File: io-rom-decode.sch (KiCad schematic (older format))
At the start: 9 parts, among them IC25 74LS02, IC26 74LS138, IC27 74LS21, IC27 74LS27, IC28 74LS20, IC29 74LS27, IC82 74LS138, IC83 74LS32

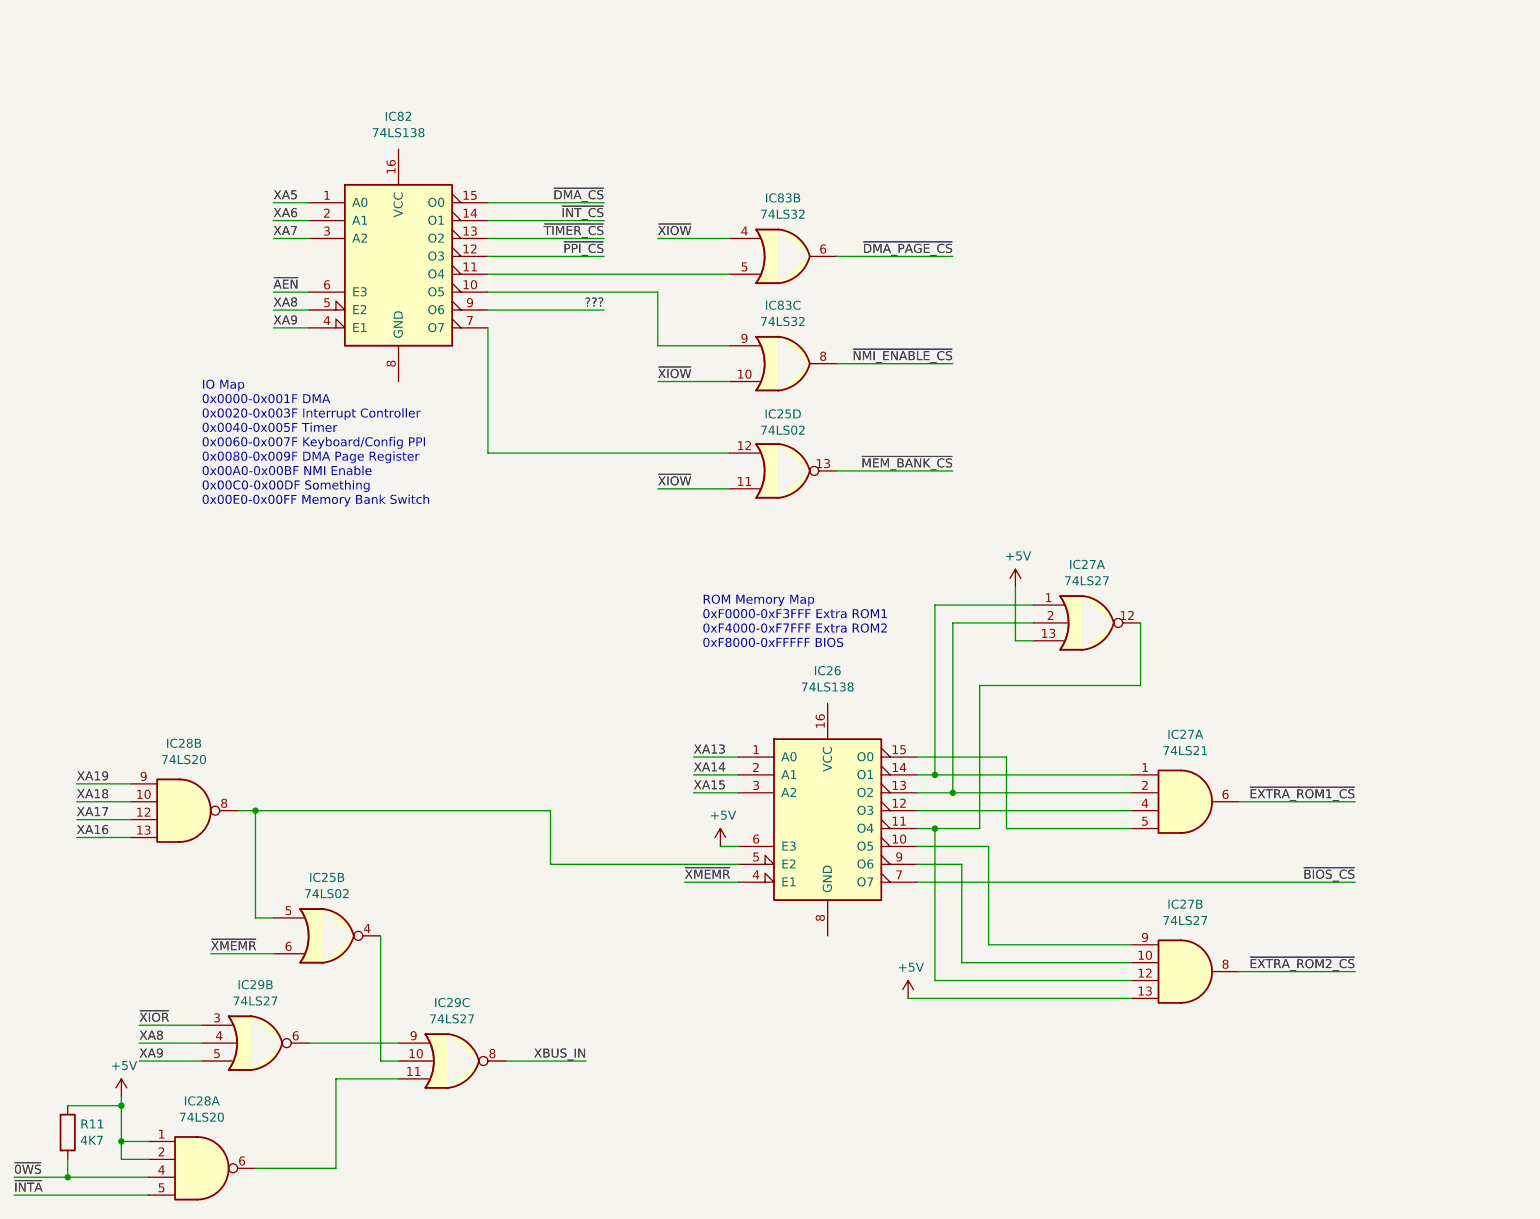
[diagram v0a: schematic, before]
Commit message: Tidy up and map all signals
This fixes up the schematic to:
 - Look presentable
 - Fix all labels connecting sheets
 - Tidy up all loose ends by either inspecting the PCB under
    magnification, measuring with an oscillosope or buzzing
    out with a meter
 - Pass ERC (with 1 exception due to incorrect circuitry around
    pin 33 on the FPU (~RQ~/~GT1~)
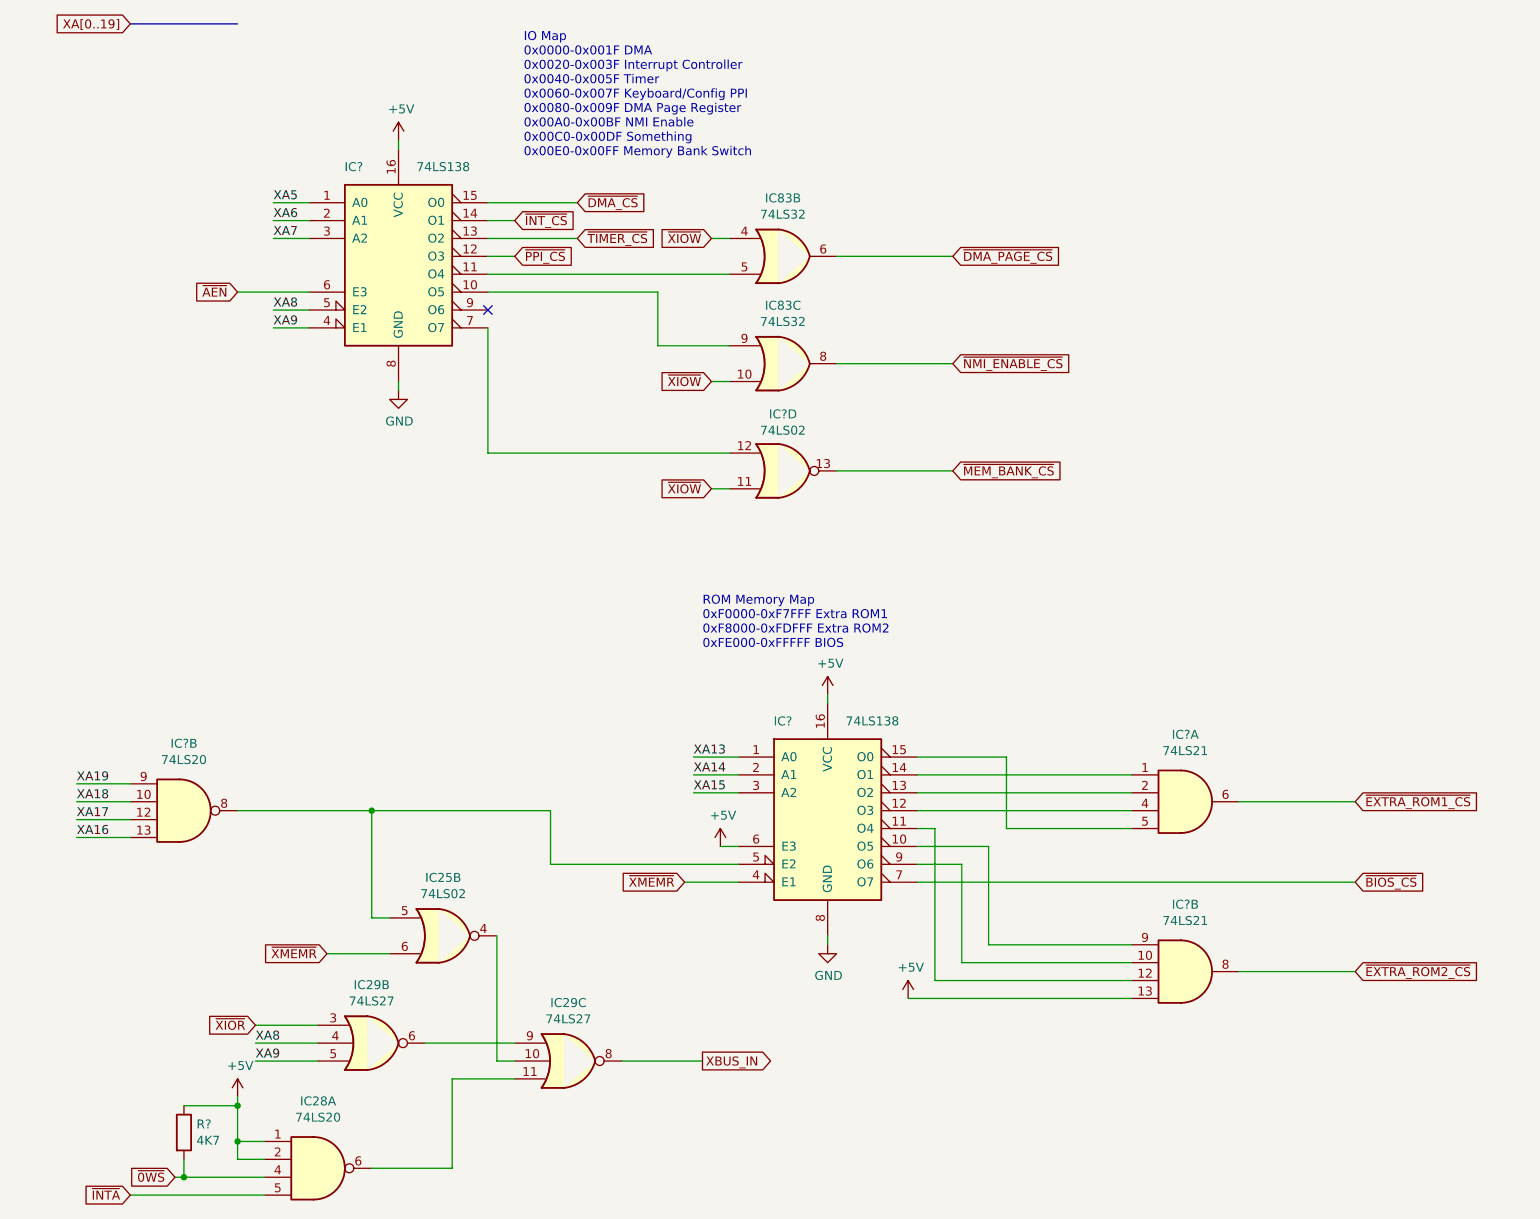
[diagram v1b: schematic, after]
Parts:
- removed IC27: 74LS27, symbol 74xx:74LS27
- removed unit 2 of IC27
- added IC?: 74LS21, symbol 74xx:74LS21
- renumbered IC25 to IC?, IC27 to IC?, IC26 to IC?, IC28 to IC?, IC82 to IC?, R11 to R?
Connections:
- net +5V: now also IC?.16 (VCC), IC?.16 (VCC), IC?.13
- net ~EXTRA_ROM2_CS~: now also IC?.8
- net at IC?.11 (O4): now also IC?.12
- net at IC?.9 (O6): now also IC?.10
- net at IC?.10 (O5): now also IC?.9
- net GND: now reaches IC?.8 (GND)
- net GND: now also IC?.8 (GND)
- net ???: no longer names the net of IC?.9 (O6)
- no-connect marks 0 -> 1
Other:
- note added: "ROM Memory Map\n0xF0000-0xF7FFF Extra ROM1\n0xF8000-0xFDFFF Extra ROM2\n0xFE000-0xFFFFF BIOS"
- note removed: "ROM Memory Map\n0xF0000-0xF3FFF Extra ROM1\n0xF4000-0xF7FFF Extra ROM2\n0xF8000-0xFFFFF BIOS"
- moved on the sheet: IC25B, IC28A, IC29B, IC29C, R?

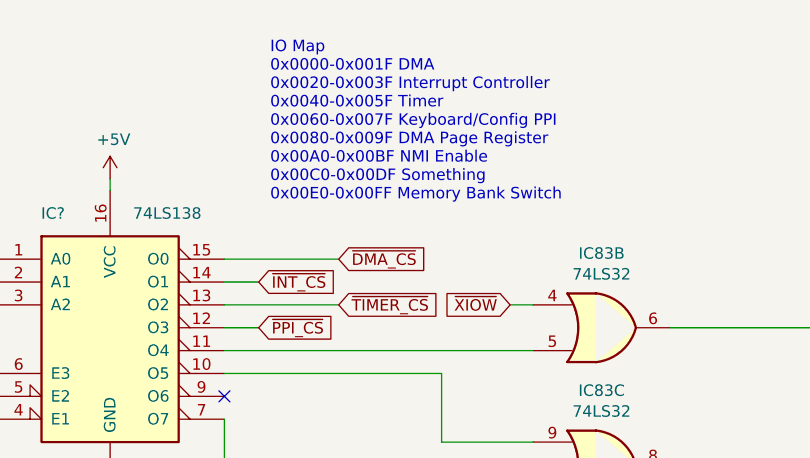
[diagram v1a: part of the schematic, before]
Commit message: Add Revision 1.0 and copyright notice
Add a simple copyright notice as this reverse engineered
schematic is all my own work. The design is still copyright
Wugo I believe.
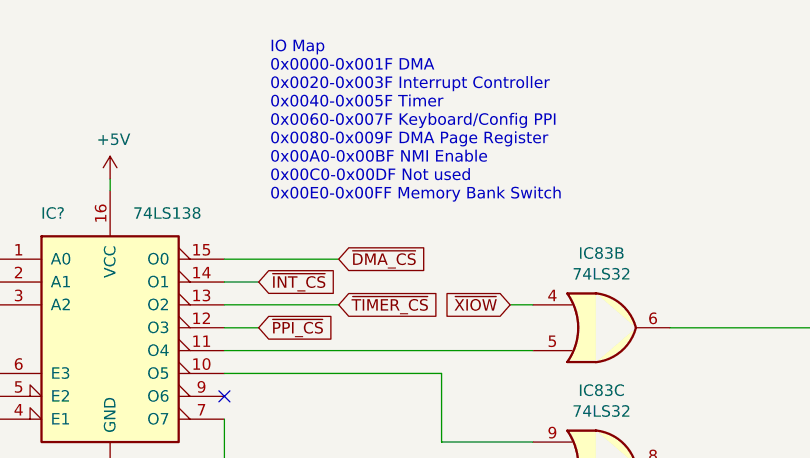
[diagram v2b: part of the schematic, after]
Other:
- note added: "IO Map\n0x0000-0x001F DMA\n0x0020-0x003F Interrupt Controller\n0x0040-0x005F Timer\n0x0060-0x007F Keyboard/Config PPI\n0x0080-0x009F DMA Page Register\n0x00A0-0x00BF NMI Enable\n0x00C0-0x00DF Not used\n0x00E0-0x00FF Memory Bank Switch"
- note removed: "IO Map\n0x0000-0x001F DMA\n0x0020-0x003F Interrupt Controller\n0x0040-0x005F Timer\n0x0060-0x007F Keyboard/Config PPI\n0x0080-0x009F DMA Page Register\n0x00A0-0x00BF NMI Enable\n0x00C0-0x00DF Something\n0x00E0-0x00FF Memory Bank Switch"
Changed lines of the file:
@@
 Title "Wugo PCII System Board"
 Date ""
-Rev ""
+Rev "1.0"
 Comp ""
-Comment1 ""
+Comment1 "Schematics Copyright (c) 2020 David J. Fiddes <D.J@fiddes.net>"
 Comment2 ""
 Comment3 ""
@@
 	3250 3350 4600 3350
 Text Notes 3450 1700 0    50   ~ 0
-IO Map\n0x0000-0x001F DMA\n0x0020-0x003F Interrupt Controller\n0x0040-0x005F Timer\n0x0060-0x007F Keyboard/Config PPI\n0x0080-0x009F DMA Page Register\n0x00A0-0x00BF NMI Enable\n0x00C0-0x00DF Something\n0x00E0-0x00FF Memory Bank Switch
+IO Map\n0x0000-0x001F DMA\n0x0020-0x003F Interrupt Controller\n0x0040-0x005F Timer\n0x0060-0x007F Keyboard/Config PPI\n0x0080-0x009F DMA Page Register\n0x00A0-0x00BF NMI Enable\n0x00C0-0x00DF Not used\n0x00E0-0x00FF Memory Bank Switch
 Wire Wire Line
 	5850 3450 5200 3450
